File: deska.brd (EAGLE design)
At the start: 65.7 x 52.1 mm, 23 parts, among them Q1 BC547, X1 JST-XH-03-PIN-LONG-PAD, X2 JST-XH-03-PIN-LONG-PAD, X3 JST-XH-03-PIN-LONG-PAD, X4 JST-XH-04-PIN-LONG-PAD, X5 JST-XH-04-PIN-LONG-PAD, X6 JST-XH-04-PIN-LONG-PAD, X7 JST-XH-03-PIN-LONG-PAD

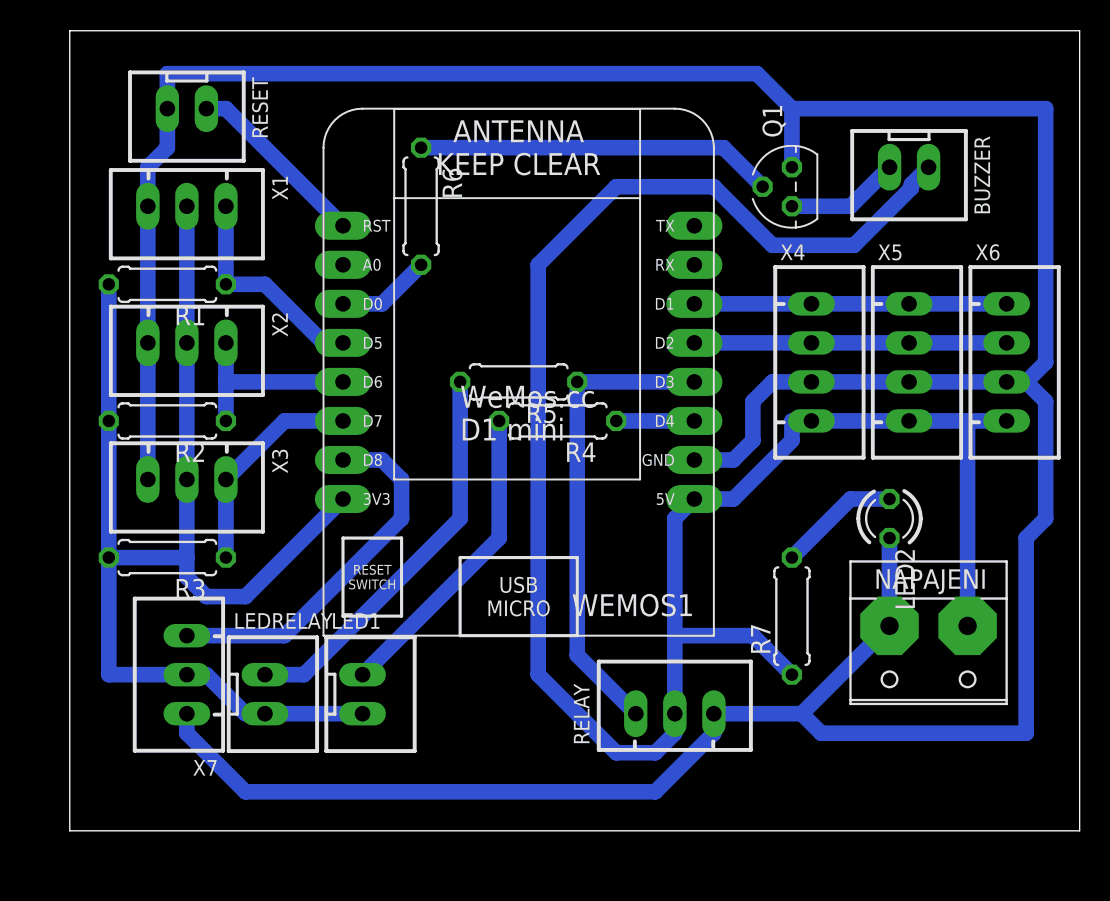
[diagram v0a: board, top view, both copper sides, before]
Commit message: deska s prohozením pinů
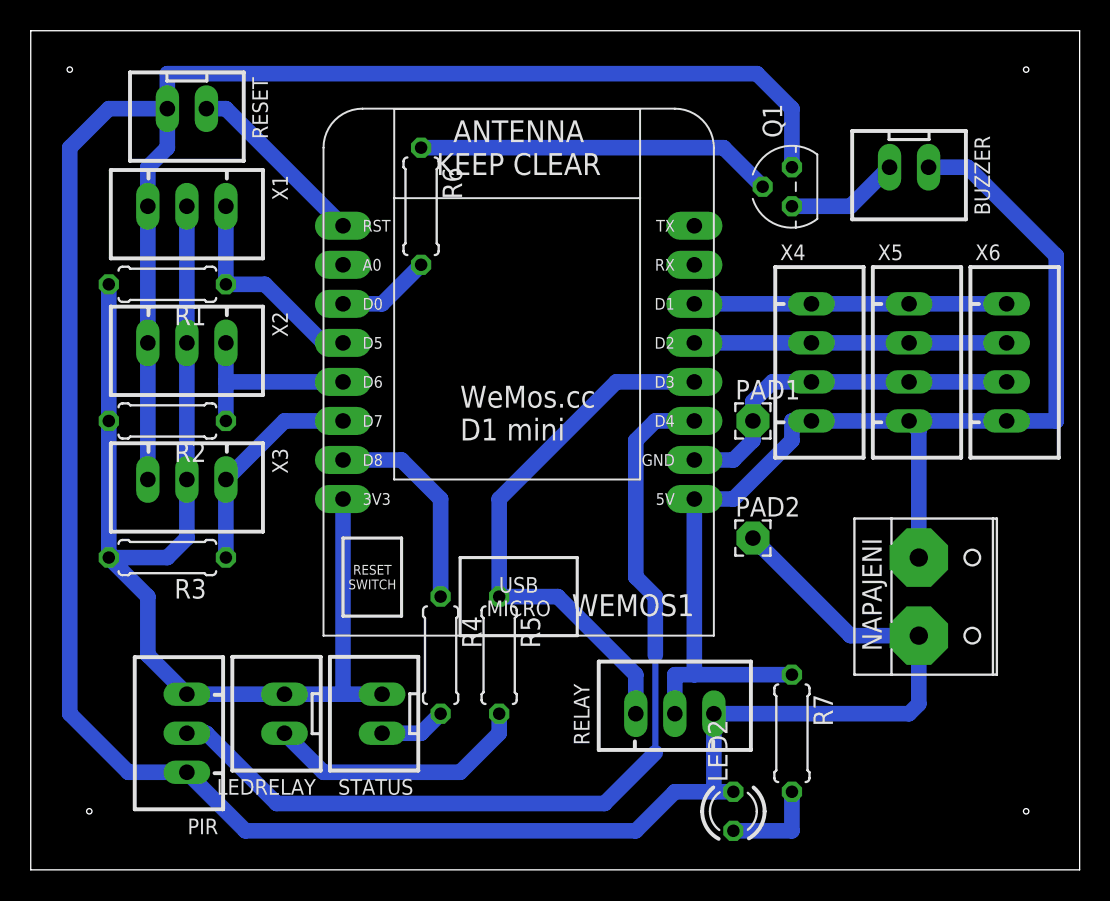
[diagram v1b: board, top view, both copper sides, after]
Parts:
- removed LED1: JST-XH-02-PIN-LONG-PAD, Rembrandt Electronics - JST XH Connectors v1-0:JST-XH-02-PACKAGE-LONG-PAD
- removed X7: JST-XH-03-PIN-LONG-PAD, Rembrandt Electronics - JST XH Connectors v1-0:JST-XH-03-PACKAGE-LONG-PAD
- added PAD1, PAD2: (no value), wirepad:2,15/1,0
- added PIR: JST-XH-03-PIN-LONG-PAD, Rembrandt Electronics - JST XH Connectors v1-0:JST-XH-03-PACKAGE-LONG-PAD
- added STATUS: JST-XH-02-PIN-LONG-PAD, Rembrandt Electronics - JST XH Connectors v1-0:JST-XH-02-PACKAGE-LONG-PAD
- moved LED2 21.6 mm to (59.7, 6.35), turned to 90 degrees
- moved R5 17.8 mm to (44.5, 16.5), turned to 270 degrees
- moved R4 17.0 mm to (40.6, 16.5), turned to 270 degrees
- moved R7 7.62 mm to (63.5, 11.4), turned to 270 degrees
- moved NAPAJENI 2.54 mm to (72.4, 20.3), turned to 270 degrees
- moved LEDRELAY 1.80 mm to (30.5, 12.7), turned to 90 degrees
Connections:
- net +3V3: now also PIR.3, STATUS.2; no longer LED1.2, X7.2
- net BUILTINLED: now also WEMOS1.D8; no longer WEMOS1.D4
- net GND: now also PAD1.1, PAD2.1, PIR.1; no longer X7.1
- net N$3: now also PIR.2, WEMOS1.D4; no longer WEMOS1.D8, X7.3
- net N$6: now also STATUS.1; no longer LED1.1
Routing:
- net +5V: track 130.5 -> 78.6 mm
- net N$3: track 24.0 -> 58.9 mm
- net N$6: track 20.2 -> 4.34 mm
- net BUILTINLED: track 5.08 -> 13.8 mm
- net N$2: track 25.8 -> 17.3 mm
- net GND: track 230.9 -> 224.4 mm
- net N$14: track 30.8 -> 35.7 mm
- net +3V3: track 85.5 -> 81.4 mm
- net N$4: track 7.93 -> 6.35 mm
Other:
- board size 65.7 x 52.1 mm -> 68.2 x 54.6 mm

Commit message: +
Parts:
- removed PAD1, PAD2: (no value), wirepad:2,15/1,0
- removed PIR: JST-XH-03-PIN-LONG-PAD, Rembrandt Electronics - JST XH Connectors v1-0:JST-XH-03-PACKAGE-LONG-PAD
- removed STATUS: JST-XH-02-PIN-LONG-PAD, Rembrandt Electronics - JST XH Connectors v1-0:JST-XH-02-PACKAGE-LONG-PAD
- added LED1: JST-XH-02-PIN-LONG-PAD, Rembrandt Electronics - JST XH Connectors v1-0:JST-XH-02-PACKAGE-LONG-PAD
- added X7: JST-XH-03-PIN-LONG-PAD, Rembrandt Electronics - JST XH Connectors v1-0:JST-XH-03-PACKAGE-LONG-PAD
- moved LED2 21.6 mm to (69.8, 25.4), turned to 270 degrees
- moved R5 17.8 mm to (45.7, 34.3), turned to 180 degrees
- moved R4 17.0 mm to (48.3, 31.8), turned to 180 degrees
- moved R7 7.62 mm to (63.5, 19.1), turned to 90 degrees
- moved NAPAJENI 2.54 mm to (72.4, 17.8), turned to 180 degrees
- moved LEDRELAY 1.80 mm to (29.2, 14.0), turned to 270 degrees
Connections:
- net +3V3: now also LED1.2, X7.2; no longer PIR.3, STATUS.2
- net BUILTINLED: now also WEMOS1.D4; no longer WEMOS1.D8
- net GND: now also X7.1; no longer PAD1.1, PAD2.1, PIR.1
- net N$3: now also WEMOS1.D8, X7.3; no longer PIR.2, WEMOS1.D4
- net N$6: now also LED1.1; no longer STATUS.1
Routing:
- net +5V: track 78.6 -> 130.5 mm
- net N$3: track 58.9 -> 24.0 mm
- net N$6: track 4.34 -> 20.2 mm
- net BUILTINLED: track 13.8 -> 5.08 mm
- net N$2: track 17.3 -> 25.8 mm
- net GND: track 224.4 -> 230.9 mm
- net N$14: track 35.7 -> 30.8 mm
- net +3V3: track 81.4 -> 85.5 mm
- net N$4: track 6.35 -> 7.93 mm
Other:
- board size 68.2 x 54.6 mm -> 65.7 x 52.1 mm
